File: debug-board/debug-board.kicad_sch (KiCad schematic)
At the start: 48 parts, among them J1 Conn_01x02_Pin, J10 Conn_01x02_Pin, J2 Conn_01x02_Pin, J3 Conn_01x02_Pin, J5 Conn_01x02_Pin, J6 Conn_01x02_Pin, J9 Conn_01x02_Pin

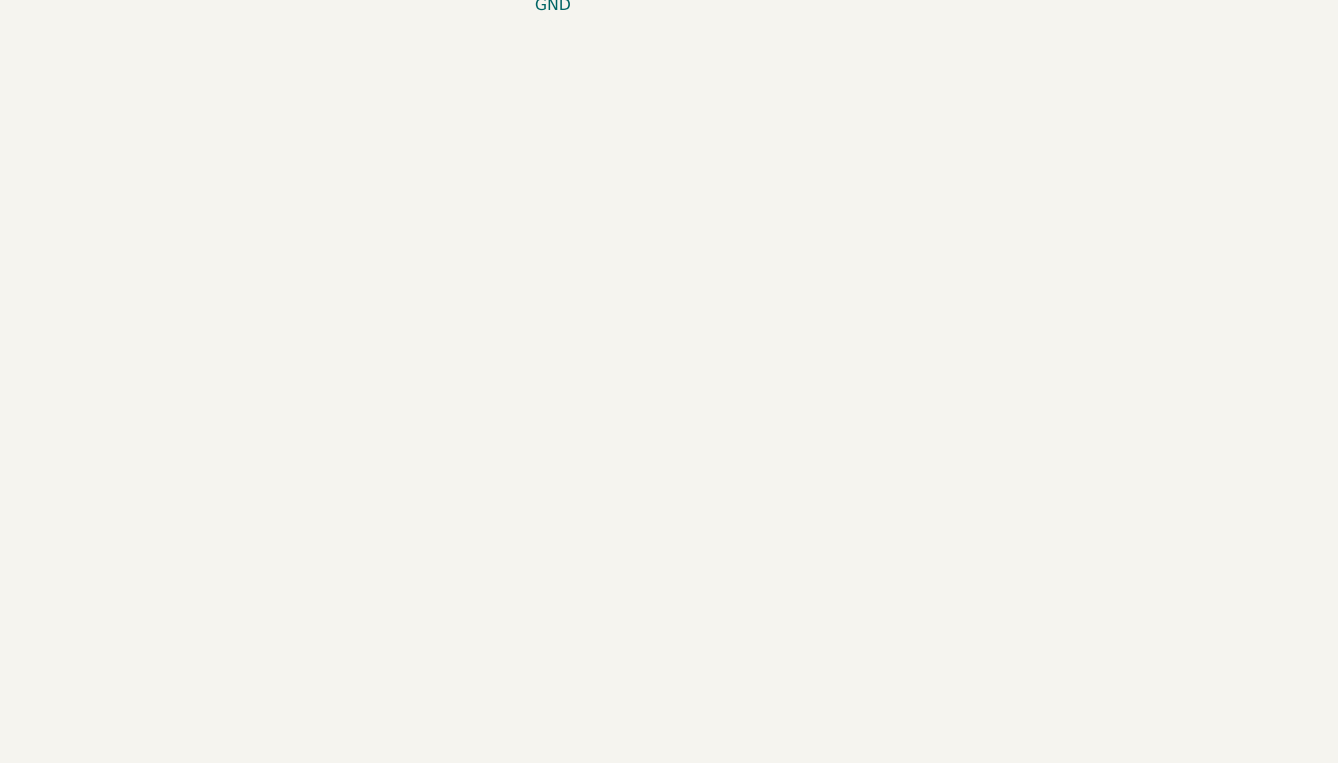
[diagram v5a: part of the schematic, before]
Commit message: Added strain gauge circuit
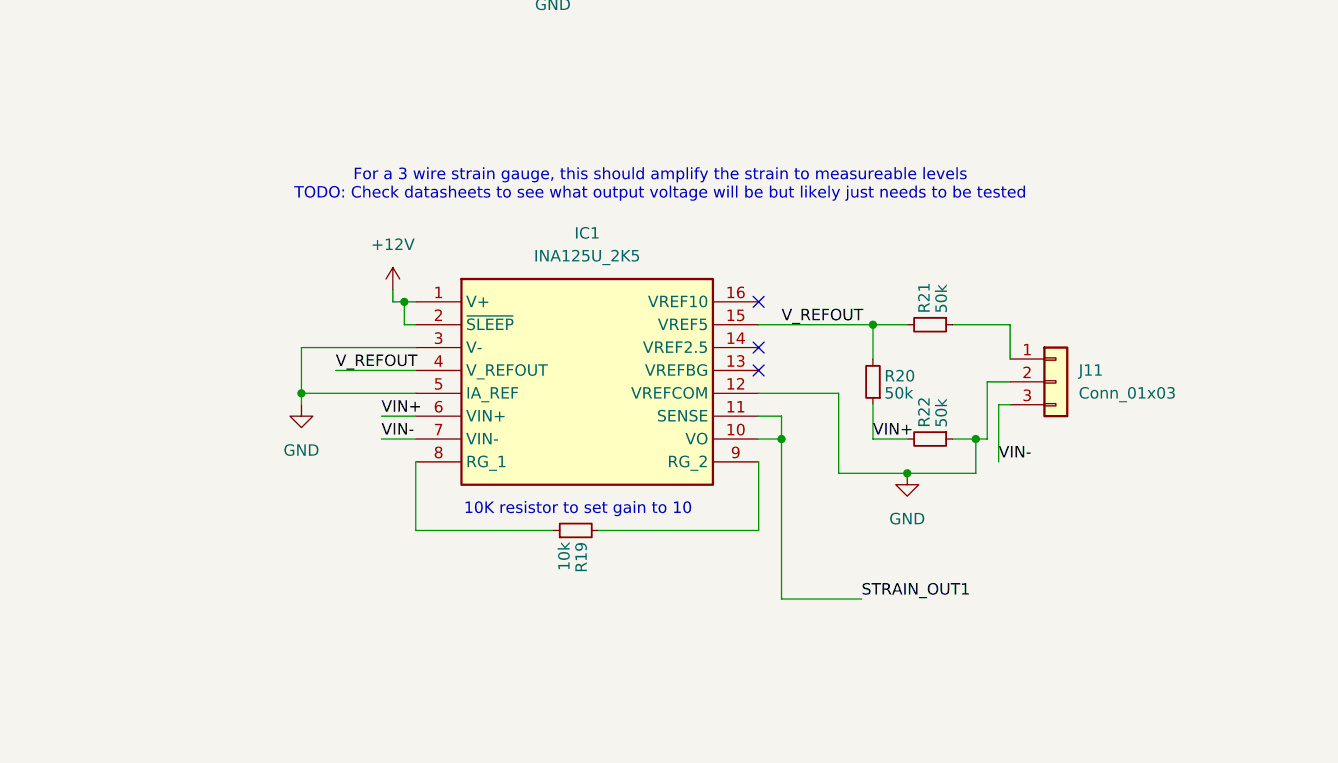
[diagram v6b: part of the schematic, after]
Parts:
- added IC1: INA125U_2K5, SOIC127P600X175-16N, symbol sufst-lib:INA125U_2K5
- added J11: Conn_01x03, symbol Connector_Generic:Conn_01x03
- added R19: 10k, Resistor_SMD:R_0805_2012Metric_Pad1.20x1.40mm_HandSolder, symbol Device:R_Small
- added R20, R21, R22: 50k, Resistor_SMD:R_0805_2012Metric_Pad1.20x1.40mm_HandSolder, symbol Device:R_Small
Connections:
- net +12V: now also IC1.1 (V+), IC1.2 (~{SLEEP})
- net GND: now also IC1.12 (VREFCOM), IC1.3 (V-), IC1.5 (IA_REF), J11.2 (Pin_2), R22.1
- new net: IC1.8 (RG_1), R19.1
- new net: IC1.9 (RG_2), R19.2
- new net: J11.1 (Pin_1), R21.1
- new net STRAIN_OUT1: IC1.10 (VO), IC1.11 (SENSE)
- new net VIN+: IC1.6 (VIN+), R20.1, R22.2
- new net VIN-: IC1.7 (VIN-), J11.3 (Pin_3)
- new net V_REFOUT: IC1.15 (VREF5), IC1.4 (V_REFOUT), R20.2, R21.2
- no-connect marks 11 -> 14
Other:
- note added: "10K resistor to set gain to 10"
- note added: "For a 3 wire strain gauge, this should amplify the strain to measureable levels TODO: Check datasheets to see what output voltage will be but likely just needs to be tested"

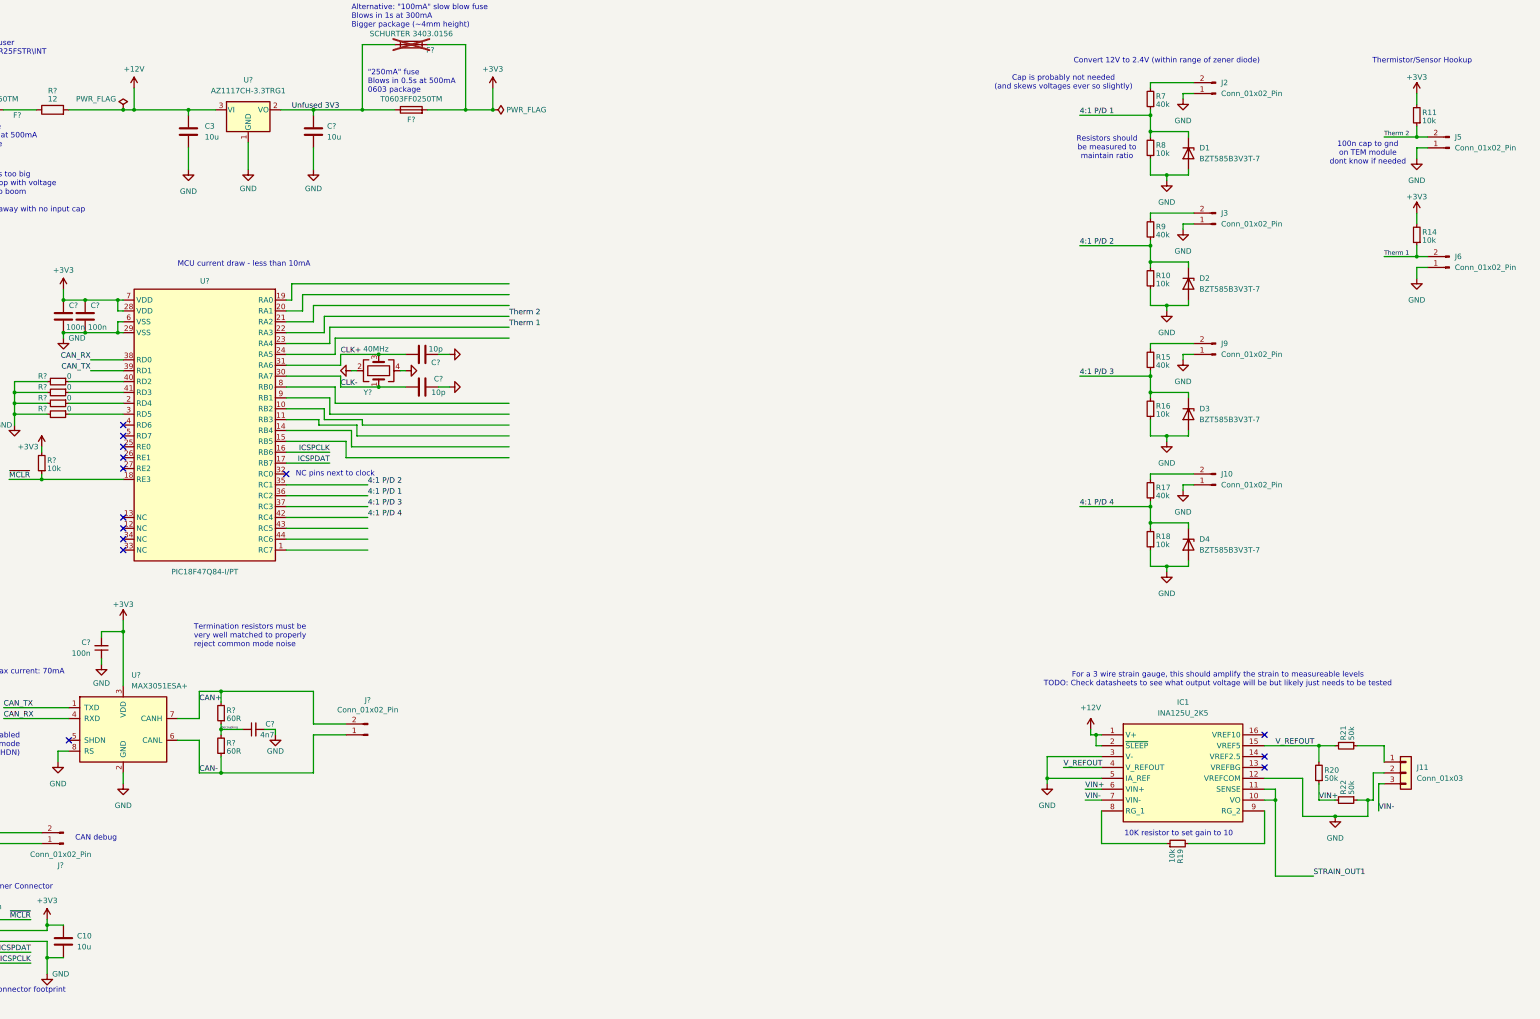
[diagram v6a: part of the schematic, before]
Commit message: Added input caps to the INA125
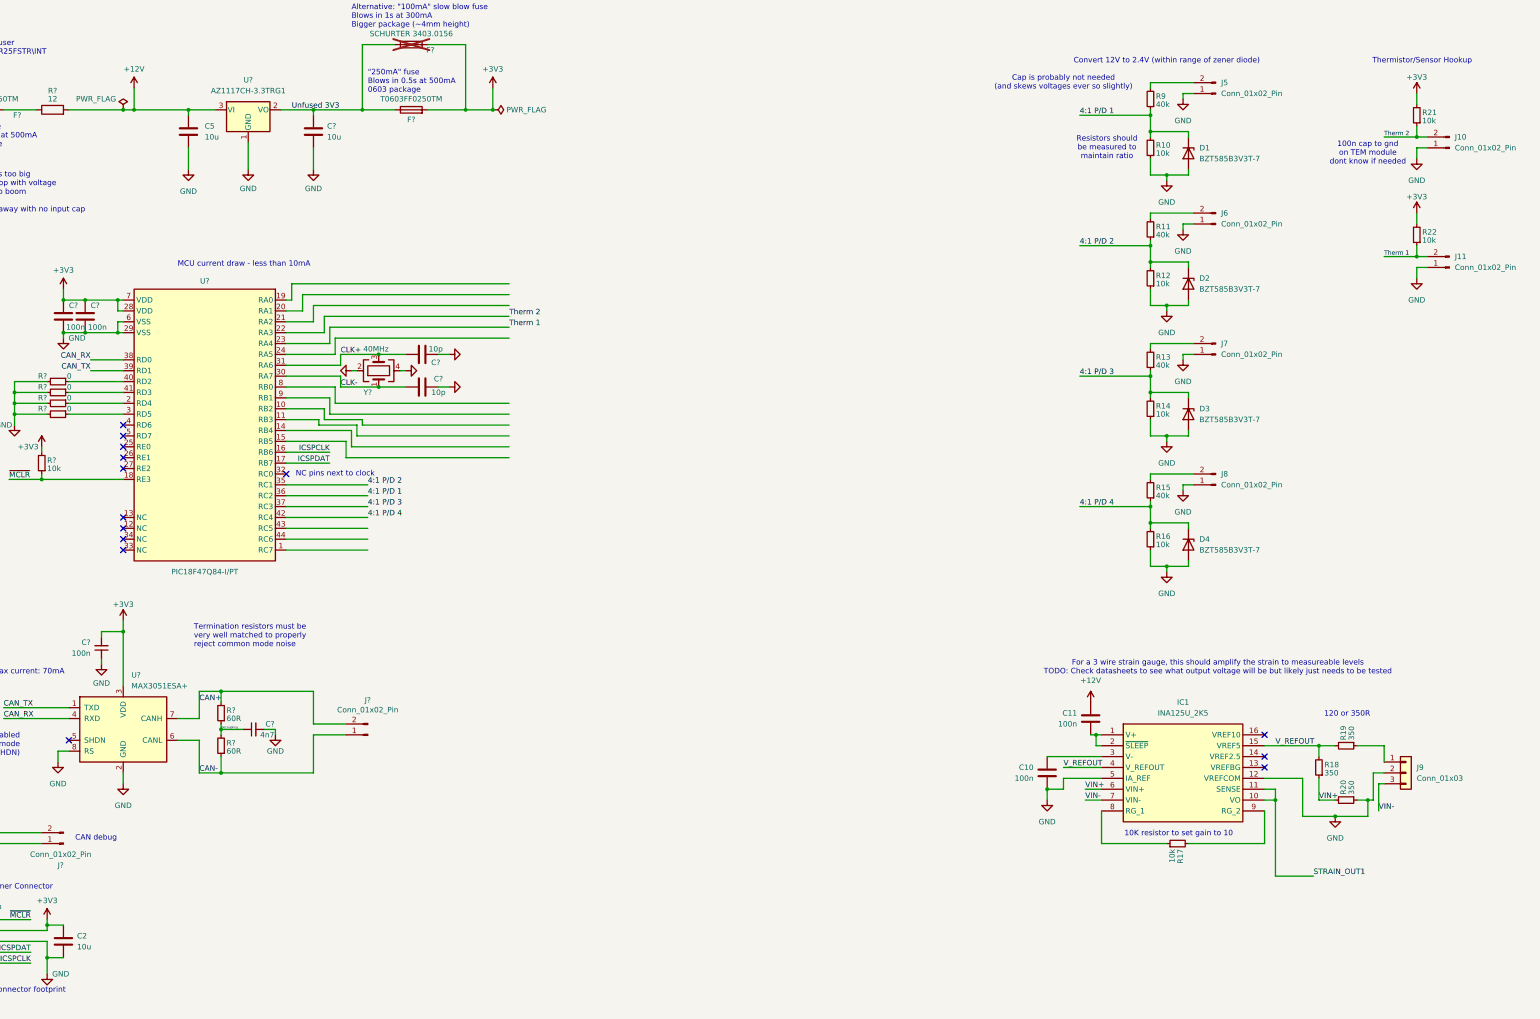
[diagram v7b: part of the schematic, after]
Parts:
- added C10, C11: 100n, Capacitor_SMD:C_0805_2012Metric_Pad1.18x1.45mm_HandSolder, symbol Device:C
- R18: renamed from R20; value 50k -> 350
- R19: renamed from R21; value 50k -> 350
- R20: renamed from R22; value 50k -> 350
- renumbered C10 to C2, C3 to C5, J5 to J10, J6 to J11, J2 to J5, J3 to J6, J9 to J7, J10 to J8, J11 to J9, R8 to R10, R9 to R11, R10 to R12, R15 to R13, R16 to R14, R17 to R15, R18 to R16, R19 to R17, R11 to R21, R14 to R22, R7 to R9
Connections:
- net +12V: now also C11.1; no longer IC1.1 (V+), IC1.2 (~{SLEEP})
- net GND: now also C10.2; no longer IC1.3 (V-)
- new net: C11.2, IC1.1 (V+), IC1.2 (~{SLEEP})
- new net: C10.1, IC1.3 (V-)
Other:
- note added: "120 or 350R"
- moved on the sheet: R18

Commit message: Initial sensor board commit
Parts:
- J9: footprint (none) -> Connector_Molex:Molex_Micro-Fit_3.0_43650-0300_1x03_P3.00mm_Horizontal
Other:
- note added: "Potential divider could be replaced with a RM2012A-103/503-PBVW10 (MAX5490TC05000-T obsolete) It would be a 5:1 divider but still in middle of ADC range (2V)"
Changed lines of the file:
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@@
 		)
 	)
+	(text "Potential divider could be replaced with a RM2012A-103/503-PBVW10 \n(MAX5490TC05000-T obsolete)\nIt would be a 5:1 divider but still in middle of ADC range (2V)"
+		(exclude_from_sim no)
+		(at 259.588 67.056 0)
+		(effects
+			(font
+				(size 1.27 1.27)
+			)
+		)
+	)
 	(text "100n cap to gnd\non TEM module\ndont know if needed"
 		(exclude_from_sim no)
@@
 			)
 		)
-		(property "Footprint" ""
+		(property "Footprint" "Connector_Molex:Molex_Micro-Fit_3.0_43650-0300_1x03_P3.00mm_Horizontal"
 			(at 372.11 193.04 0)
 			(effects
